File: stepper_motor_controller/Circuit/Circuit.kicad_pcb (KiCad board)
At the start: 2 copper layers, 16 parts, among them SW1 SW_Push_SPDT, U1 LM7805_TO220, U2 TMC2209_SILENTSTEPSTICK

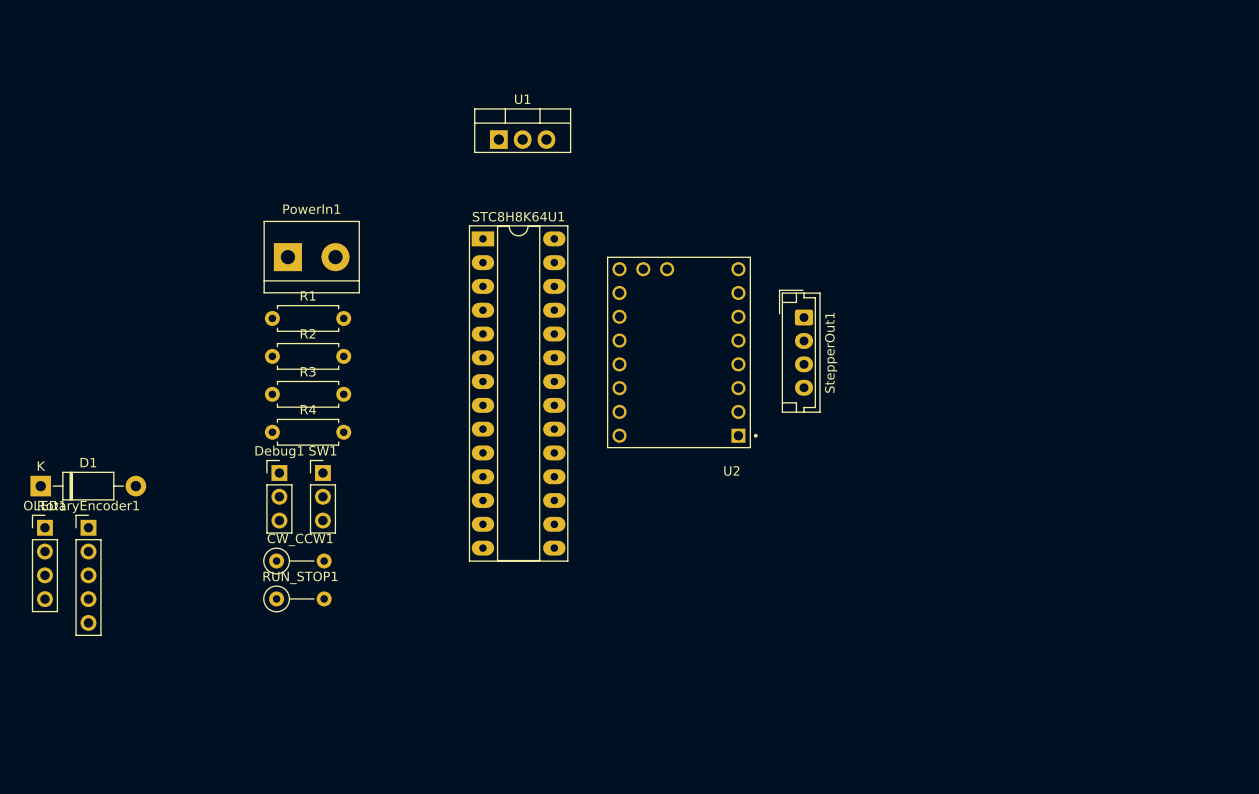
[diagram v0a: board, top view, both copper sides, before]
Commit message: stepper motor controller circuit moredevelopment and started the programming
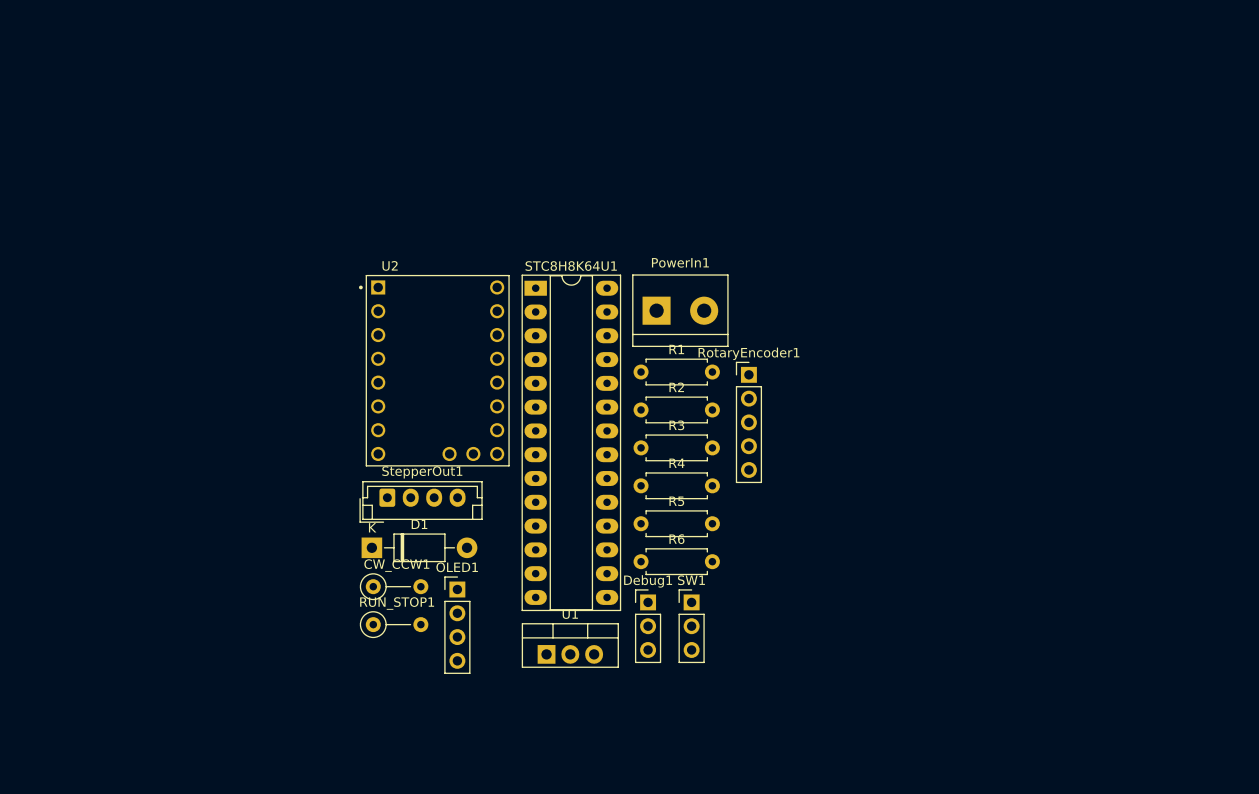
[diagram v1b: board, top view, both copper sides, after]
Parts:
- added R5: 200, Resistor_THT:R_Axial_DIN0207_L6.3mm_D2.5mm_P7.62mm_Horizontal, F.Cu at (151.6, 107.0)
- added R6: 330, Resistor_THT:R_Axial_DIN0207_L6.3mm_D2.5mm_P7.62mm_Horizontal, F.Cu at (151.6, 111.1)
- U1: value LM7805_TO220 -> LM317_TO-220
- moved RotaryEncoder1 72.4 mm to (163.1, 91.1)
- moved U1 55.2 mm to (141.5, 121.0)
- moved StepperOut1 48.5 mm to (124.5, 104.2), turned to 0 degrees
- moved OLED1 44.5 mm to (132.0, 114.0)
- moved Debug1 41.7 mm to (152.3, 115.4)
- moved SW1 41.7 mm to (157.0, 115.4)
- moved PowerIn1 39.8 mm to (153.3, 84.3)
- moved R1 39.8 mm to (151.6, 90.8)
- moved R2 39.8 mm to (151.6, 94.9)
- moved R3 39.8 mm to (151.6, 98.9)
- moved R4 39.8 mm to (151.6, 103.0)
- moved D1 36.0 mm to (122.9, 109.6)
- moved U2 25.8 mm to (129.9, 90.7), turned to 0 degrees
- moved RUN_STOP1 10.7 mm to (123.0, 117.8)
- moved CW_CCW1 10.7 mm to (123.0, 113.7)
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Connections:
- OLED1 pad 3: unconnected-(OLED1-Pin_3-Pad3) -> +3.3V
- R2 pad 2: unconnected-(R2-Pad2) -> +3.3V
- R3 pad 2: unconnected-(R3-Pad2) -> +3.3V
- R4 pad 2: unconnected-(R4-Pad2) -> +3.3V
- RotaryEncoder1 pad 4: unconnected-(RotaryEncoder1-Pin_4-Pad4) -> +3.3V
- U1 pad 1: +24V -> Net-(U1-ADJ)
- U1 pad 2: GND -> +3.3V
- U1 pad 3: +5V -> +24V
- U2 pad 2: unconnected-(U2-VIO-Pad2) -> +3.3V
- U2 pad 8: unconnected-(U2-VM-Pad8) -> +24V

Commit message: finished buttons switches and encoder interfacing for stepper driver
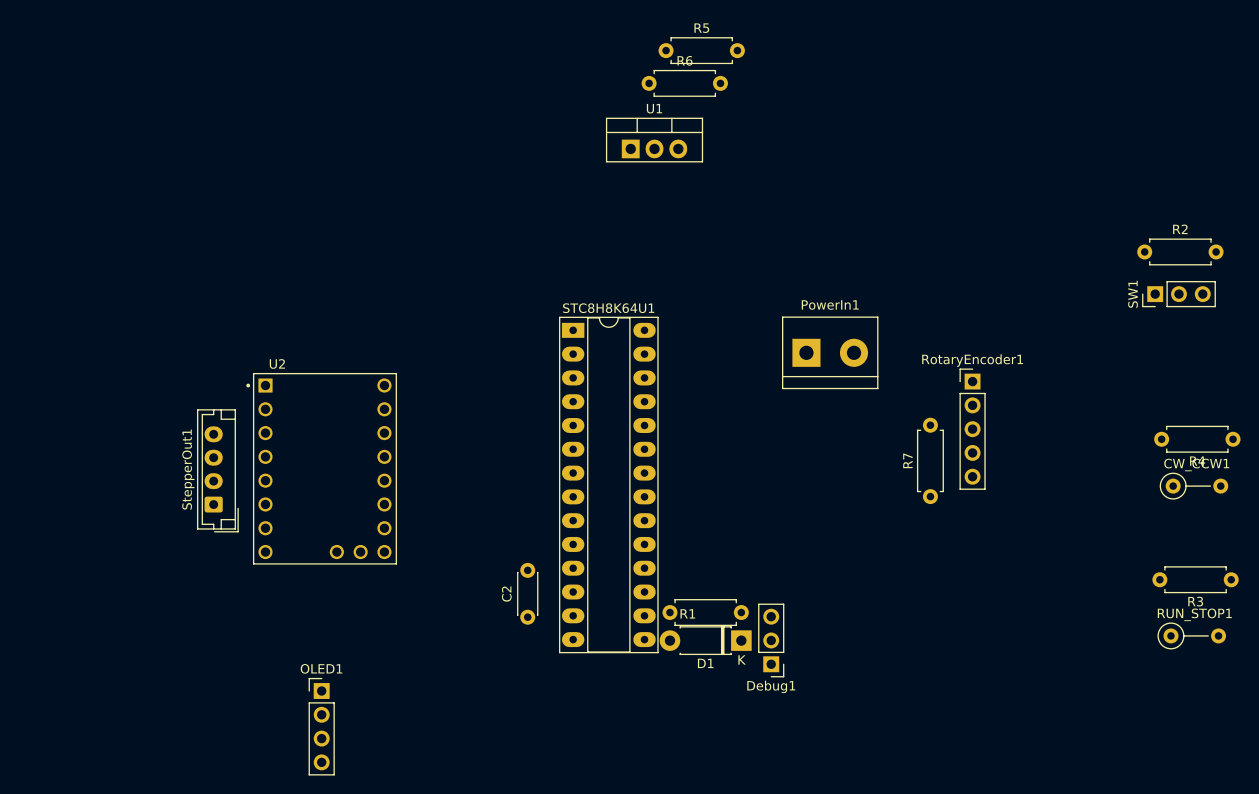
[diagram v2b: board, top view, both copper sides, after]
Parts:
- added C2: 10nf, Capacitor_THT:C_Disc_D4.3mm_W1.9mm_P5.00mm, F.Cu at (139.5, 117.0)
- added R7: 10k, Resistor_THT:R_Axial_DIN0207_L6.3mm_D2.5mm_P7.62mm_Horizontal, F.Cu at (182.5, 104.1)
- D1: footprint Diode_THT:D_DO-41_SOD81_P10.16mm_Horizontal -> Diode_THT:D_DO-41_SOD81_P7.62mm_Horizontal
- moved CW_CCW1 86.1 mm to (208.4, 103.0)
- moved RUN_STOP1 85.2 mm to (208.2, 119.0)
- moved R3 64.6 mm to (214.6, 113.0), turned to 180 degrees
- moved R4 63.4 mm to (214.8, 98.0), turned to 180 degrees
- moved SW1 59.4 mm to (206.5, 82.5), turned to 90 degrees
- moved R2 56.4 mm to (205.4, 78.0)
- moved U1 54.7 mm to (150.5, 67.0)
- moved R6 51.1 mm to (152.5, 60.0)
- moved R5 50.6 mm to (154.3, 56.5)
- moved D1 40.7 mm to (162.3, 119.5), turned to 180 degrees
- moved R1 25.9 mm to (154.7, 116.5)
- moved RotaryEncoder1 23.9 mm to (187.0, 91.8)
- moved StepperOut1 18.6 mm to (106.0, 105.0), turned to 90 degrees
- moved OLED1 18.1 mm to (117.5, 124.9)
- moved PowerIn1 16.6 mm to (169.3, 88.8)
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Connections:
- STC8H8K64U1 pad 10: unconnected-(STC8H8K64U1-Pin_10-Pad10) -> Net-(STC8H8K64U1-Pin_10)
- STC8H8K64U1 pad 12: unconnected-(STC8H8K64U1-Pin_12-Pad12) -> +3.3V
- STC8H8K64U1 pad 14: unconnected-(STC8H8K64U1-Pin_14-Pad14) -> GND
- U2 pad 14: unconnected-(U2-MS2-Pad14) -> MS2
- U2 pad 15: unconnected-(U2-MS1-Pad15) -> MS1

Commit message: added stepper motor driver and finished PCB
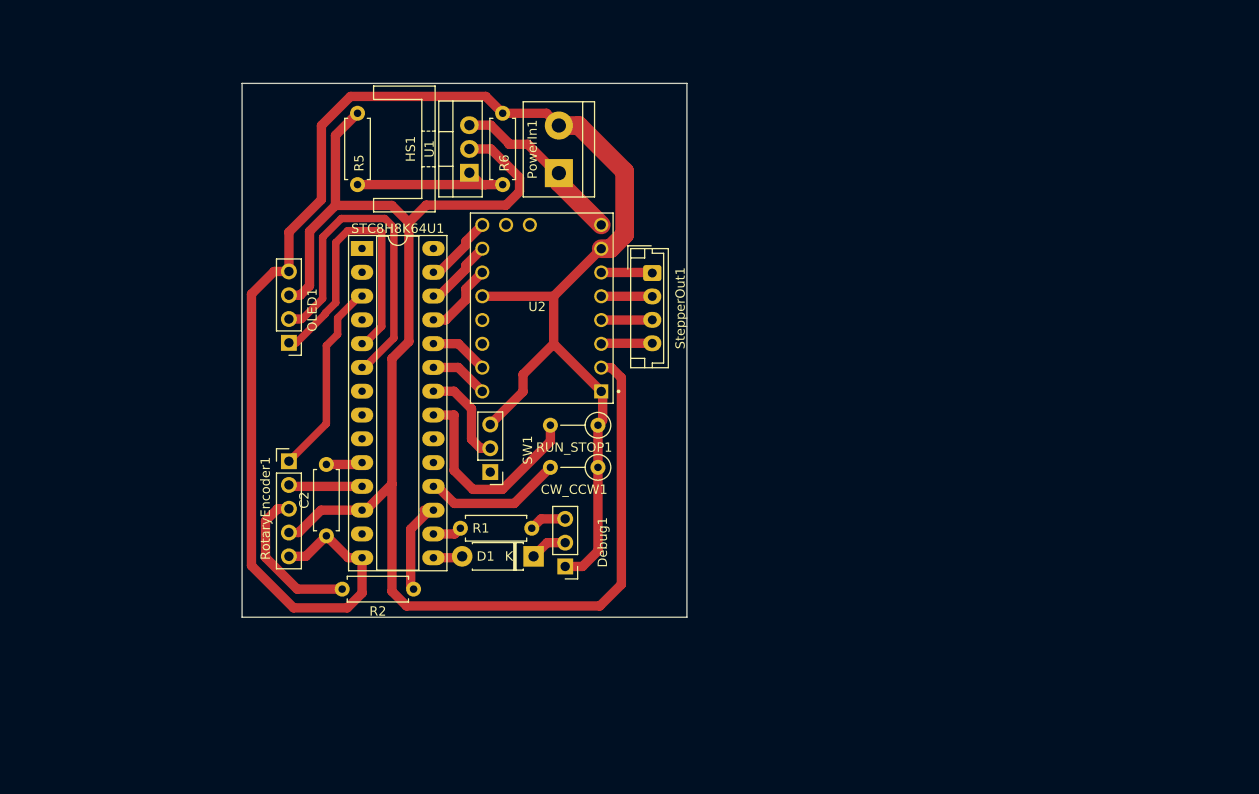
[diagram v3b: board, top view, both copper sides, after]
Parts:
- removed R3, R4, R7: 10k, Resistor_THT:R_Axial_DIN0207_L6.3mm_D2.5mm_P7.62mm_Horizontal
- added HS1: Heatsink, Heatsink:Heatsink_Stonecold_HS-S01_13.21x6.35mm, F.Cu at (129.5, 67.0)
- C2: footprint Capacitor_THT:C_Disc_D4.3mm_W1.9mm_P5.00mm -> Resistor_THT:R_Axial_DIN0207_L6.3mm_D2.5mm_P7.62mm_Horizontal
- R2: value 10k -> 0
- SW1: value SW_Push_SPDT -> SW_SPDT
- moved R2 86.0 mm to (127.3, 114.0), turned to 180 degrees
- moved SW1 73.5 mm to (135.5, 101.5), turned to 180 degrees
- moved RotaryEncoder1 73.5 mm to (114.0, 100.3)
- moved RUN_STOP1 65.2 mm to (147.0, 96.5), turned to 180 degrees
- moved CW_CCW1 61.5 mm to (147.0, 101.0), turned to 180 degrees
- moved StepperOut1 53.0 mm to (152.8, 80.2), turned to -90 degrees
- moved OLED1 37.3 mm to (114.0, 87.7), turned to 180 degrees
- moved R5 35.9 mm to (121.3, 70.8), turned to 90 degrees
- moved PowerIn1 32.7 mm to (142.8, 69.6), turned to 90 degrees
- moved U2 28.8 mm to (141.0, 84.0), turned to 180 degrees
- moved Debug1 24.4 mm to (143.5, 111.6)
- moved STC8H8K64U1 24.2 mm to (121.8, 77.6)
- moved R1 24.1 mm to (132.3, 107.5)
- moved D1 23.9 mm to (140.1, 110.5)
- moved C2 23.2 mm to (118.0, 108.3)
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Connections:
- OLED1 pad 2: SCK -> SCL
- R2 pad 1: Net-(SW1-A) -> Net-(STC8H8K64U1-Pin_17)
- R2 pad 2: +3.3V -> Encoder_Switch
- STC8H8K64U1 pad 11: unconnected-(STC8H8K64U1-Pin_11-Pad11) -> Encoder_DT
- STC8H8K64U1 pad 17: unconnected-(STC8H8K64U1-Pin_17-Pad17) -> Net-(STC8H8K64U1-Pin_17)
- STC8H8K64U1 pad 18: unconnected-(STC8H8K64U1-Pin_18-Pad18) -> CW_CCW
- STC8H8K64U1 pad 21: unconnected-(STC8H8K64U1-Pin_21-Pad21) -> RUN_STOP
- STC8H8K64U1 pad 22: unconnected-(STC8H8K64U1-Pin_22-Pad22) -> Motor_HOLD
- STC8H8K64U1 pad 23: unconnected-(STC8H8K64U1-Pin_23-Pad23) -> DIR
- STC8H8K64U1 pad 24: unconnected-(STC8H8K64U1-Pin_24-Pad24) -> STEP
- STC8H8K64U1 pad 25: unconnected-(STC8H8K64U1-Pin_25-Pad25) -> MS2
- STC8H8K64U1 pad 26: unconnected-(STC8H8K64U1-Pin_26-Pad26) -> MS1
- STC8H8K64U1 pad 27: unconnected-(STC8H8K64U1-Pin_27-Pad27) -> EN
- STC8H8K64U1 pad 3: unconnected-(STC8H8K64U1-Pin_3-Pad3) -> Encoder_CLK
- STC8H8K64U1 pad 5: unconnected-(STC8H8K64U1-Pin_5-Pad5) -> SDA
- STC8H8K64U1 pad 6: unconnected-(STC8H8K64U1-Pin_6-Pad6) -> SCL
- SW1 pad 1: Net-(SW1-A) -> unconnected-(SW1-A-Pad1)
- U2 pad 13: unconnected-(U2-SPRD-Pad13) -> GND
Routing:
- net GND: track 0.00 -> 185.6 mm
- net +3.3V: track 0.00 -> 157.1 mm
- net SCL: track 0.00 -> 36.4 mm
- net SDA: track 0.00 -> 31.8 mm
- net RUN_STOP: track 0.00 -> 23.1 mm
- net Encoder_CLK: track 0.00 -> 21.0 mm
- net +24V: track 0.00 -> 19.1 mm
- net Net-(U1-ADJ): track 0.00 -> 17.8 mm
- net Encoder_Switch: track 0.00 -> 16.5 mm
- net CW_CCW: track 0.00 -> 14.8 mm
- net Net-(STC8H8K64U1-Pin_17): track 0.00 -> 10.8 mm
- net Motor_HOLD: track 0.00 -> 10.5 mm
- net MS2: track 0.00 -> 8.00 mm
- net Encoder_DT: track 0.00 -> 7.87 mm
- net EN: track 0.00 -> 7.56 mm
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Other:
- board outline added: 47.5 x 57 mm

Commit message: huge progress in programming in stepper_motor_controller project
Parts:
- added C3: 470uf, Capacitor_THT:CP_Radial_D8.0mm_P3.50mm, F.Cu at (149.5, 67.0)
- added H1: 3.3mm, MountingHole:MountingHole_3.2mm_M3, F.Cu at (113.0, 65.5)
- added H2: 3.3mm, MountingHole:MountingHole_3.2mm_M3, F.Cu at (154.0, 113.5)
- moved StepperOut1 1.20 mm to (154.0, 80.2)
- moved R1 0.50 mm to (132.3, 107.0)
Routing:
- net +24V: track 19.1 -> 28.6 mm
- net GND: track 185.6 -> 192.2 mm
- net Net-(StepperOut1-Pin_4): track 5.47 -> 6.67 mm
- net Net-(StepperOut1-Pin_3): track 5.46 -> 6.66 mm
- net Net-(StepperOut1-Pin_2): track 5.46 -> 6.66 mm
- net Net-(StepperOut1-Pin_1): track 5.47 -> 6.67 mm
- net Net-(STC8H8K64U1-Pin_17): track 10.8 -> 9.80 mm
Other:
- board size 47.5 x 57 mm -> 49 x 57 mm
